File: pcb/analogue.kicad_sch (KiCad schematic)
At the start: 32 parts, among them U6 TLV9061xDBV, U7 TLV76150DCY, U8 TLV9061xDBV

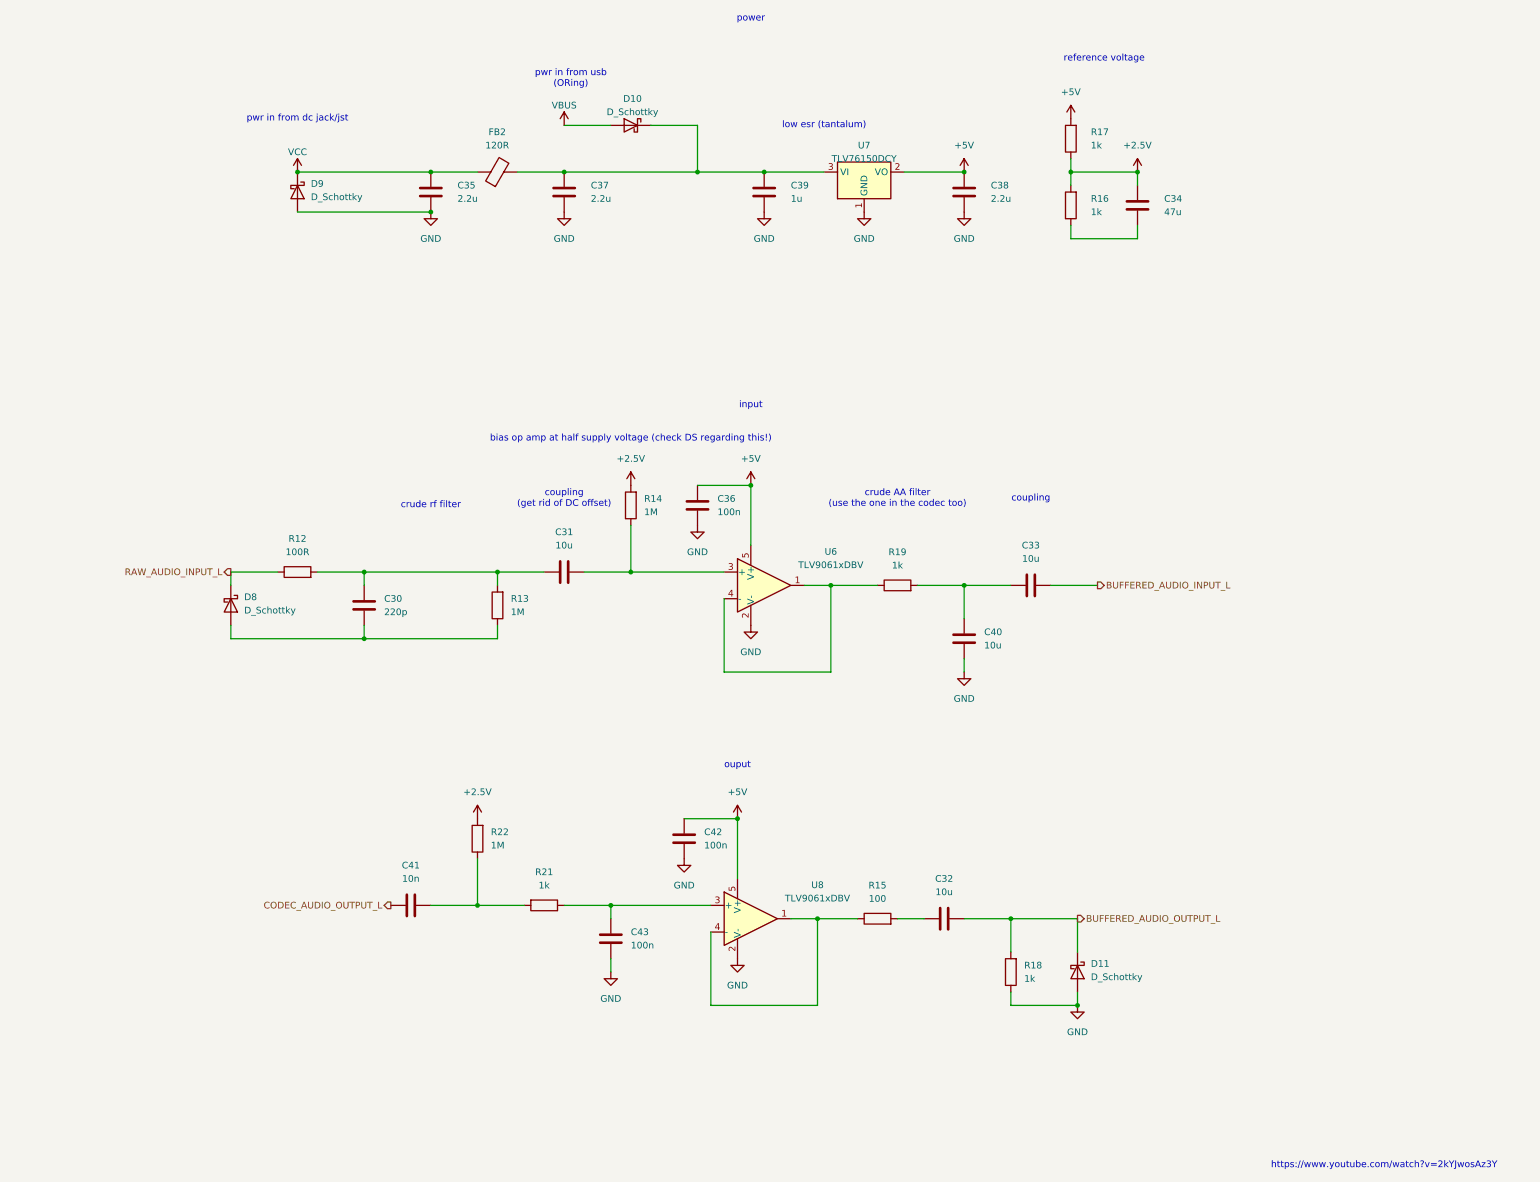
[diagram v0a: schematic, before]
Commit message: more schematic stuff, preliminary footprint choices and parts grouping, played with multicahnnel for the buttons
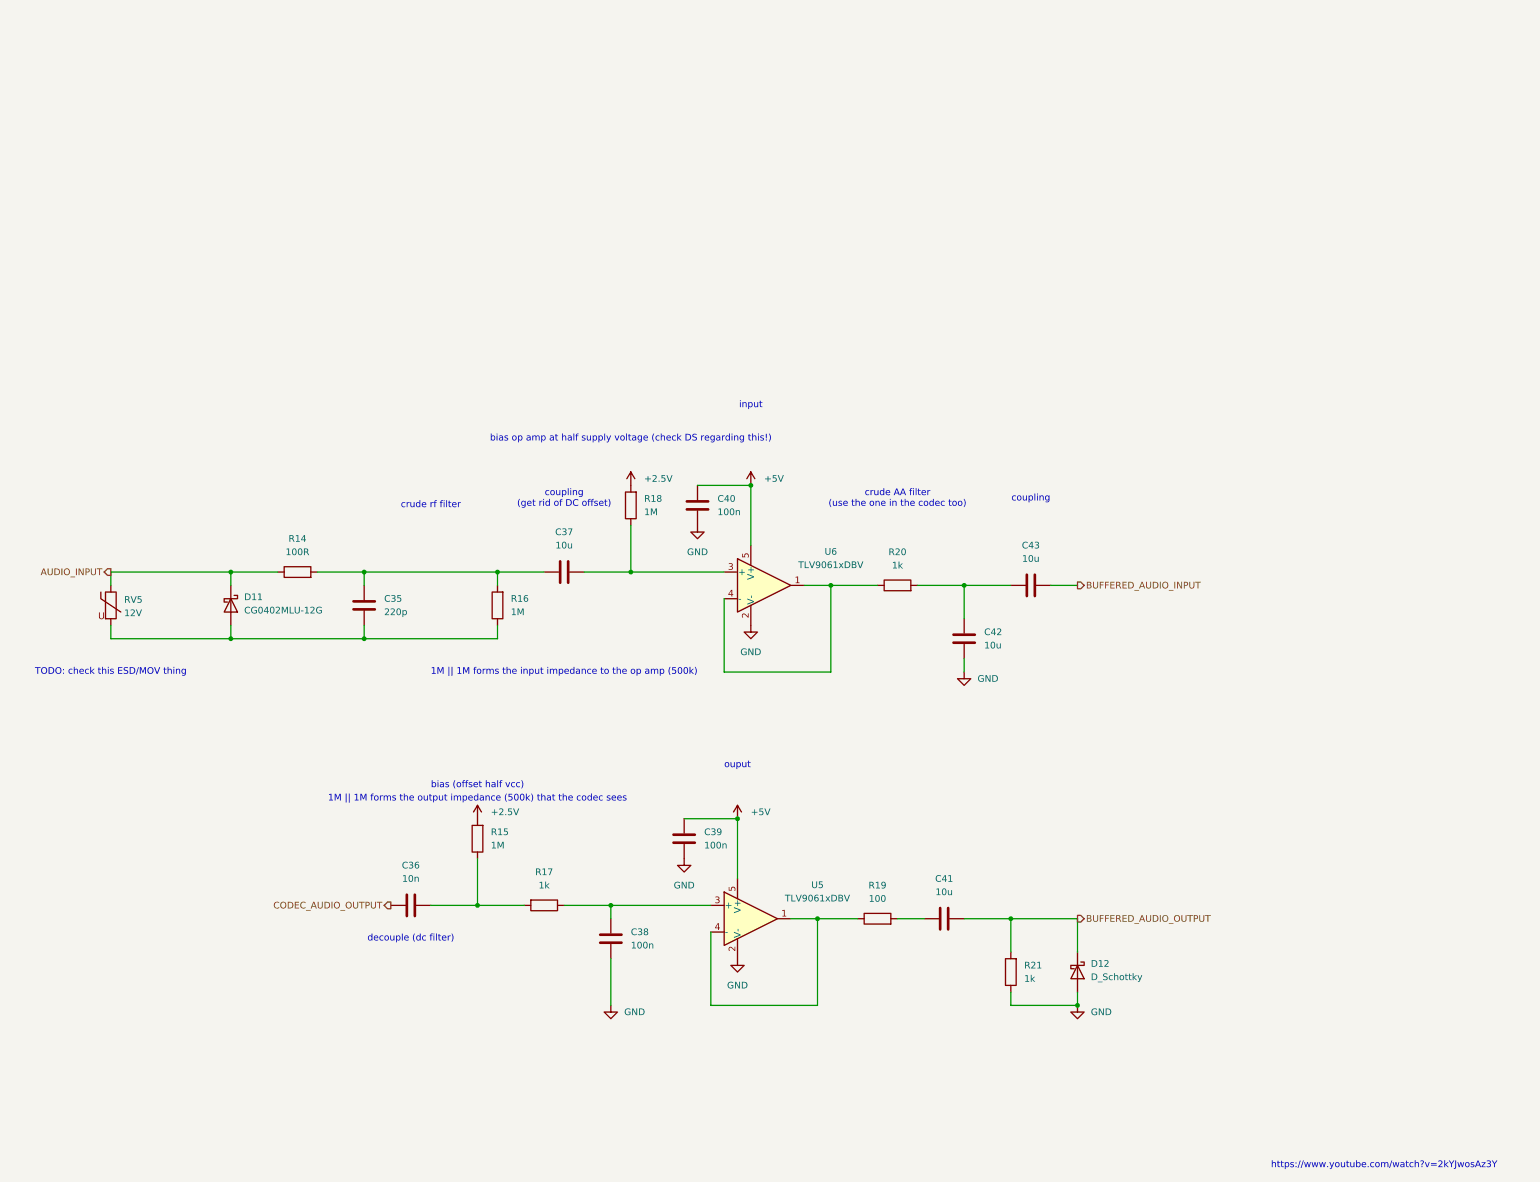
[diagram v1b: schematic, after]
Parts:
- removed C34: 47u, symbol Device:C
- removed C35, C37, C38: 2.2u, Capacitor_SMD:C_0603_1608Metric, symbol Device:C
- removed C39: 1u, Capacitor_SMD:C_0603_1608Metric, symbol Device:C
- removed D10, D9: D_Schottky, symbol Device:D_Schottky
- removed FB2: 120R, Resistor_SMD:R_0603_1608Metric, symbol Device:FerriteBead
- removed R16, R17: 1k, symbol Device:R
- removed U7: TLV76150DCY, Package_TO_SOT_SMD:SOT-223-3_TabPin2, symbol Regulator_Linear:TLV76150DCY
- added RV5: 12V, Varistor:RV_Disc_D7mm_W3.4mm_P5mm, symbol Device:Varistor
- C35: renamed from C30; footprint (none) -> Capacitor_SMD:C_0603_1608Metric
- C36: renamed from C41; footprint (none) -> Capacitor_SMD:C_0603_1608Metric
- C37: renamed from C31; footprint (none) -> Capacitor_SMD:C_0603_1608Metric
- C38: renamed from C43; footprint (none) -> Capacitor_SMD:C_0603_1608Metric
- C39: renamed from C42; footprint (none) -> Capacitor_SMD:C_0603_1608Metric
- C40: renamed from C36; footprint (none) -> Capacitor_SMD:C_0603_1608Metric
- C41: renamed from C32; footprint (none) -> Capacitor_SMD:C_0603_1608Metric
- C42: renamed from C40; footprint (none) -> Capacitor_SMD:C_0603_1608Metric
- C43: renamed from C33; footprint (none) -> Capacitor_SMD:C_0603_1608Metric
- D11: renamed from D8; value D_Schottky -> CG0402MLU-12G; footprint (none) -> Diode_SMD:D_SOD-123
- D12: renamed from D11; footprint (none) -> Diode_SMD:D_SOD-123
- R14: renamed from R12; footprint (none) -> Resistor_SMD:R_0603_1608Metric_Pad0.98x0.95mm_HandSolder
- R15: renamed from R22; footprint (none) -> Resistor_SMD:R_0603_1608Metric_Pad0.98x0.95mm_HandSolder
- R16: renamed from R13; footprint (none) -> Resistor_SMD:R_0603_1608Metric_Pad0.98x0.95mm_HandSolder
- R17: renamed from R21; footprint (none) -> Resistor_SMD:R_0603_1608Metric_Pad0.98x0.95mm_HandSolder
- R18: renamed from R14; footprint (none) -> Resistor_SMD:R_0603_1608Metric_Pad0.98x0.95mm_HandSolder
- R19: renamed from R15; footprint (none) -> Resistor_SMD:R_0603_1608Metric_Pad0.98x0.95mm_HandSolder
- R20: renamed from R19; footprint (none) -> Resistor_SMD:R_0603_1608Metric_Pad0.98x0.95mm_HandSolder
- R21: renamed from R18; footprint (none) -> Resistor_SMD:R_0603_1608Metric_Pad0.98x0.95mm_HandSolder
- renumbered U8 to U5
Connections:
- net at C35.2, D11.2 (A), R16.1: now also RV5.2
- net BUFFERED_AUDIO_INPUT_L renamed BUFFERED_AUDIO_INPUT
- net BUFFERED_AUDIO_OUTPUT_L renamed BUFFERED_AUDIO_OUTPUT
- net CODEC_AUDIO_OUTPUT_L renamed CODEC_AUDIO_OUTPUT
- net RAW_AUDIO_INPUT_L renamed AUDIO_INPUT
- net AUDIO_INPUT: now also RV5.1
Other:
- note added: "1M || 1M forms the input impedance to the op amp (500k)"
- note added: "1M || 1M forms the output impedance (500k) that the codec sees"
- note added: "TODO: check this ESD/MOV thing"
- note added: "bias (offset half vcc)"
- note added: "decouple (dc filter)"
- note removed: "low esr (tantalum)"
- note removed: "power"
- note removed: "pwr in from dc jack/jst"
- note removed: "pwr in from usb (ORing)"
- note removed: "reference voltage"

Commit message: expand usb, piano keys, cleanup
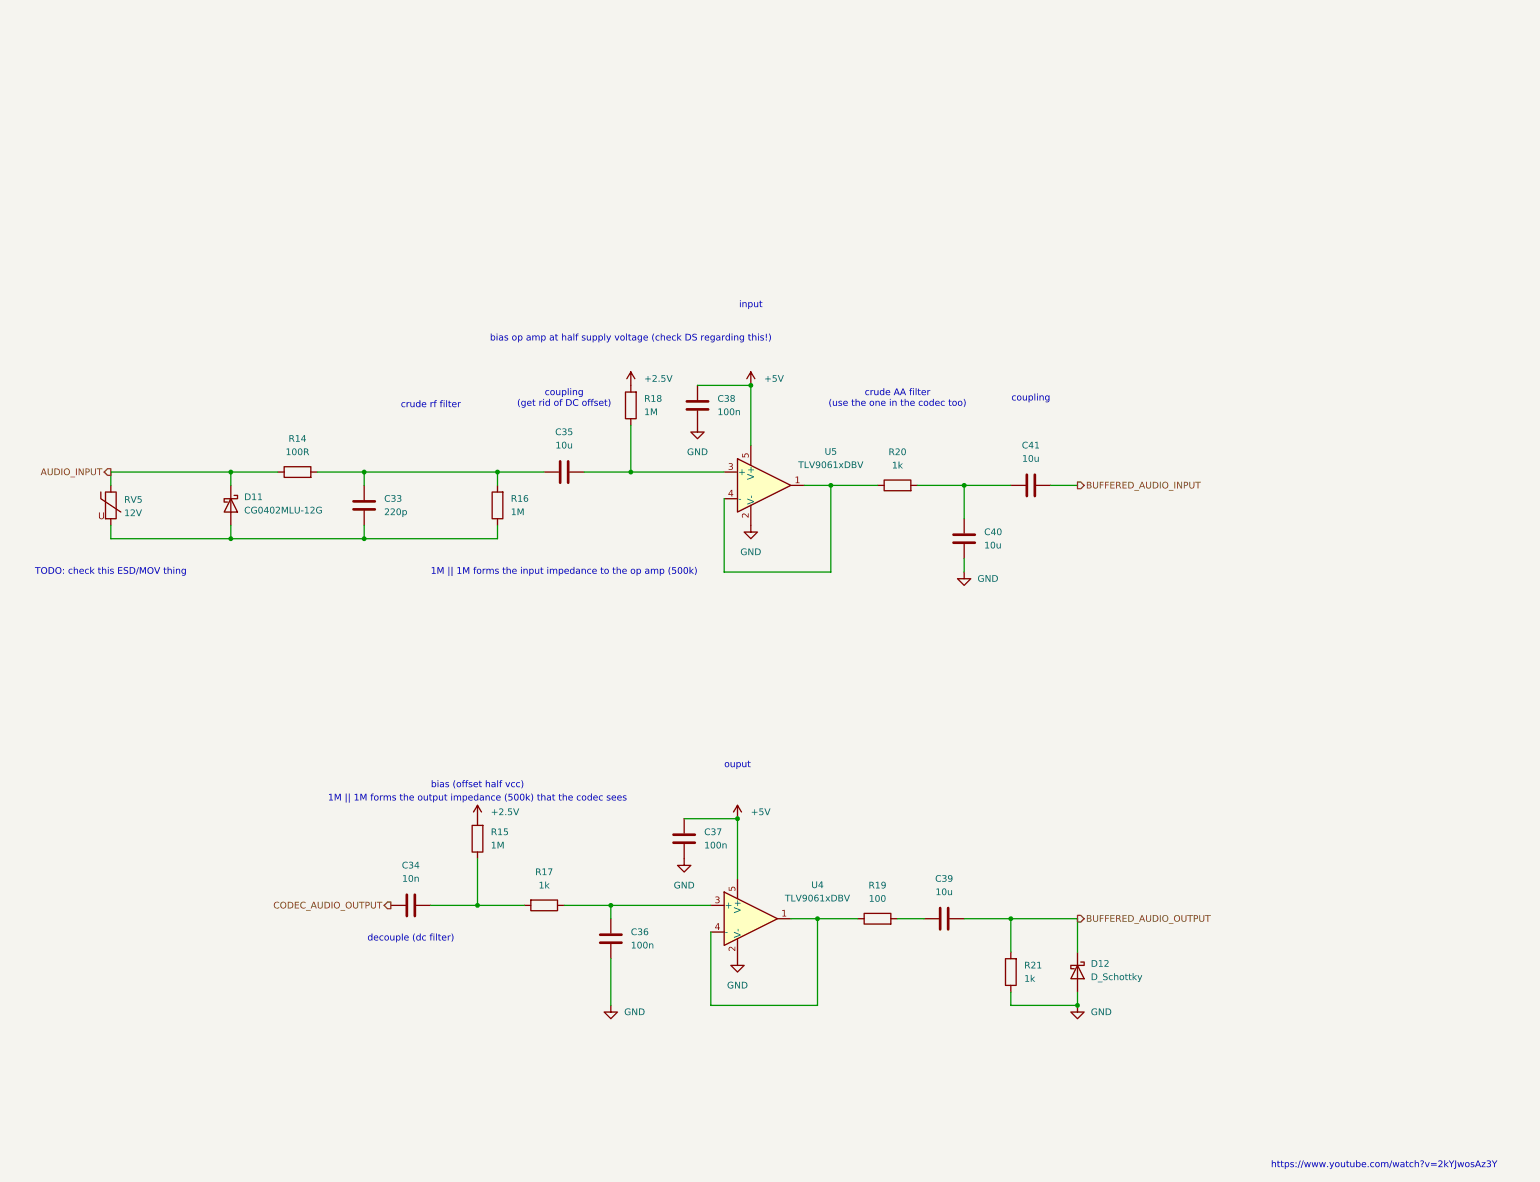
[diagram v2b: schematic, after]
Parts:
- renumbered C35 to C33, C36 to C34, C37 to C35, C38 to C36, C39 to C37, C40 to C38, C41 to C39, C42 to C40, C43 to C41, U5 to U4, U6 to U5
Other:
- moved on the sheet: C33, C35, C38, C40, C41, D11, R14, R16, R18, R20, RV5, U5

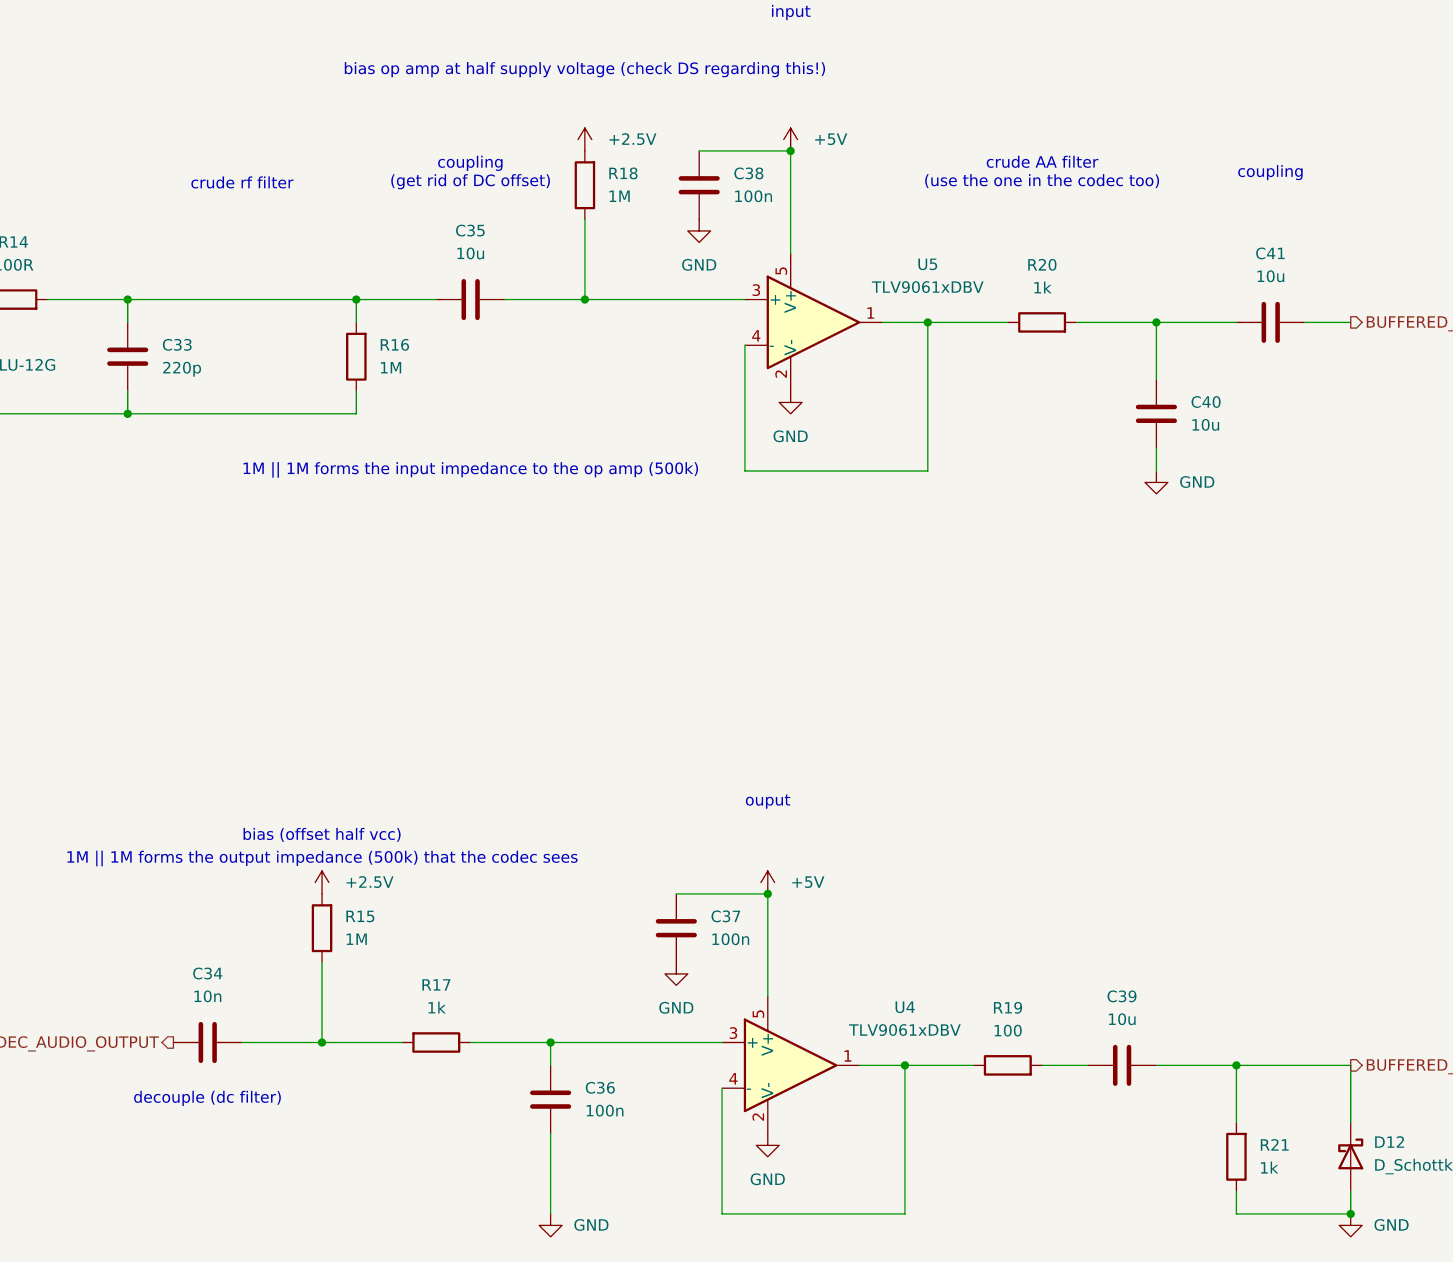
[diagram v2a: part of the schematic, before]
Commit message: switch back to rp2350, ideal diode OR'ing for power
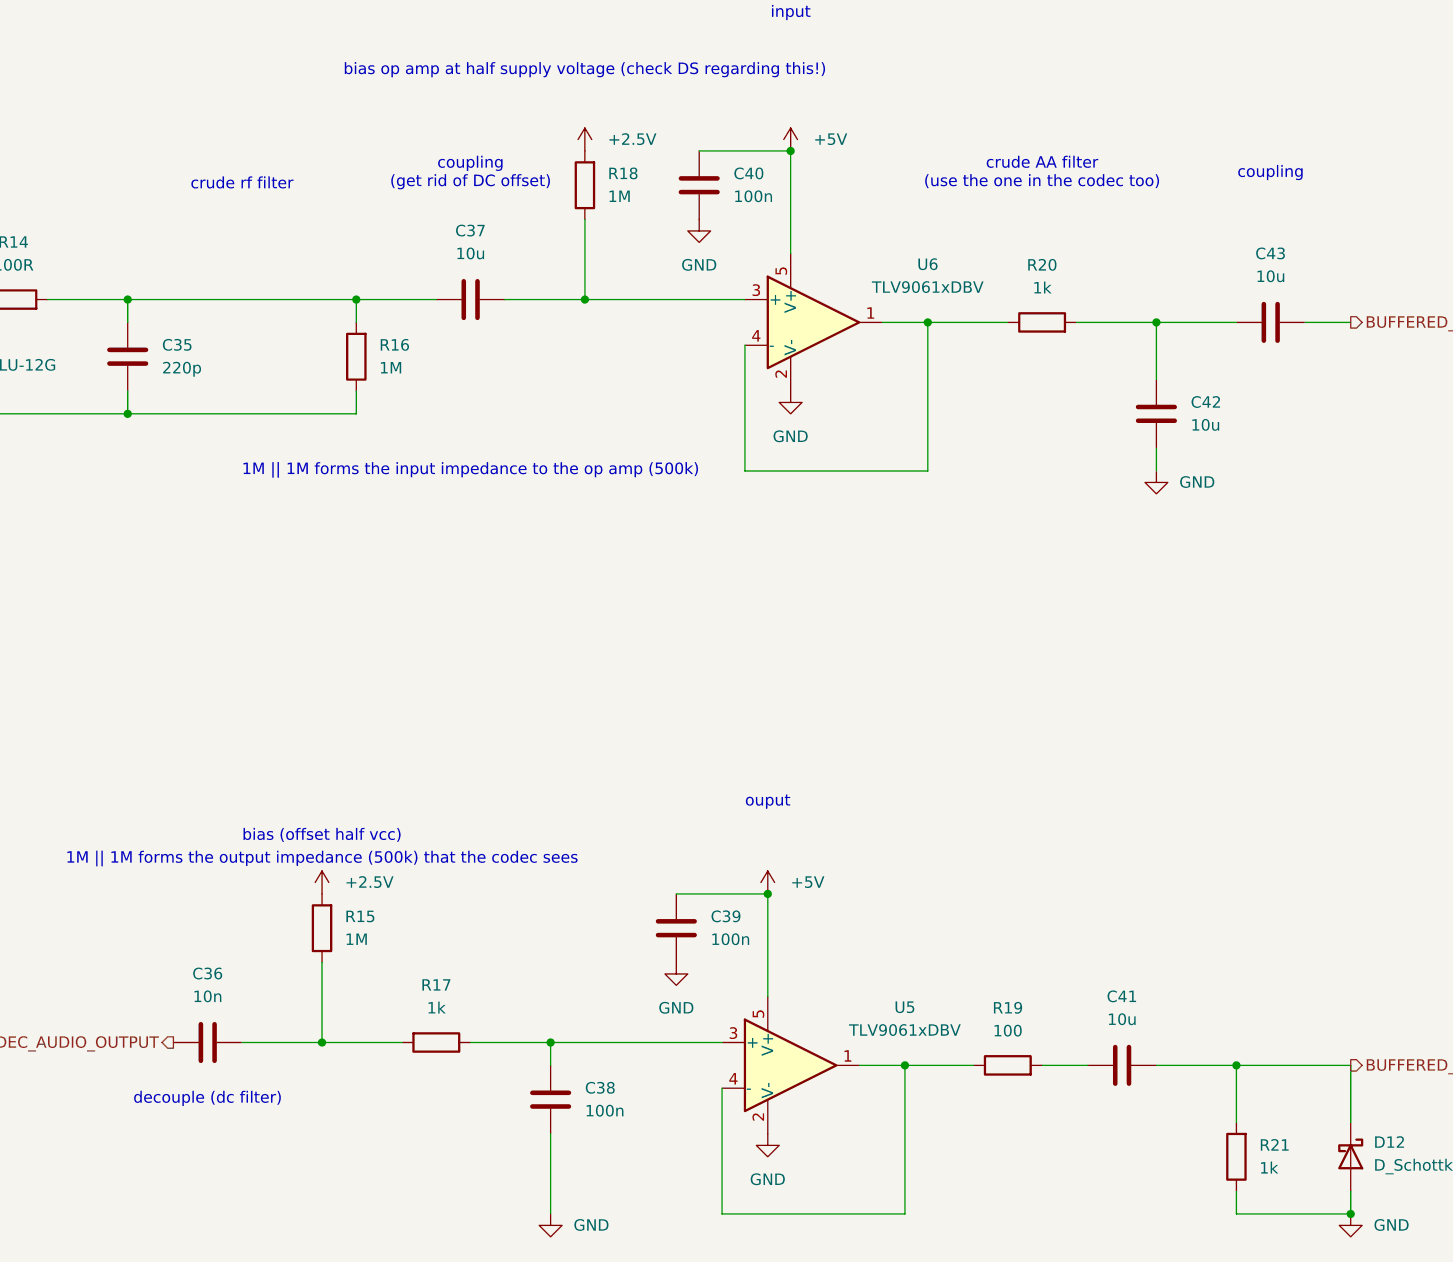
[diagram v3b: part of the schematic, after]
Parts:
- renumbered C33 to C35, C34 to C36, C35 to C37, C36 to C38, C37 to C39, C38 to C40, C39 to C41, C40 to C42, C41 to C43, U4 to U5, U5 to U6
